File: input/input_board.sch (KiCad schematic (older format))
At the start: 21 parts, among them J2 MCLK, J4 SCKA, J5 SCKB, J6 SDOB1, U1 DS90LV048, U2 FIN1047, U5 74LVC541A

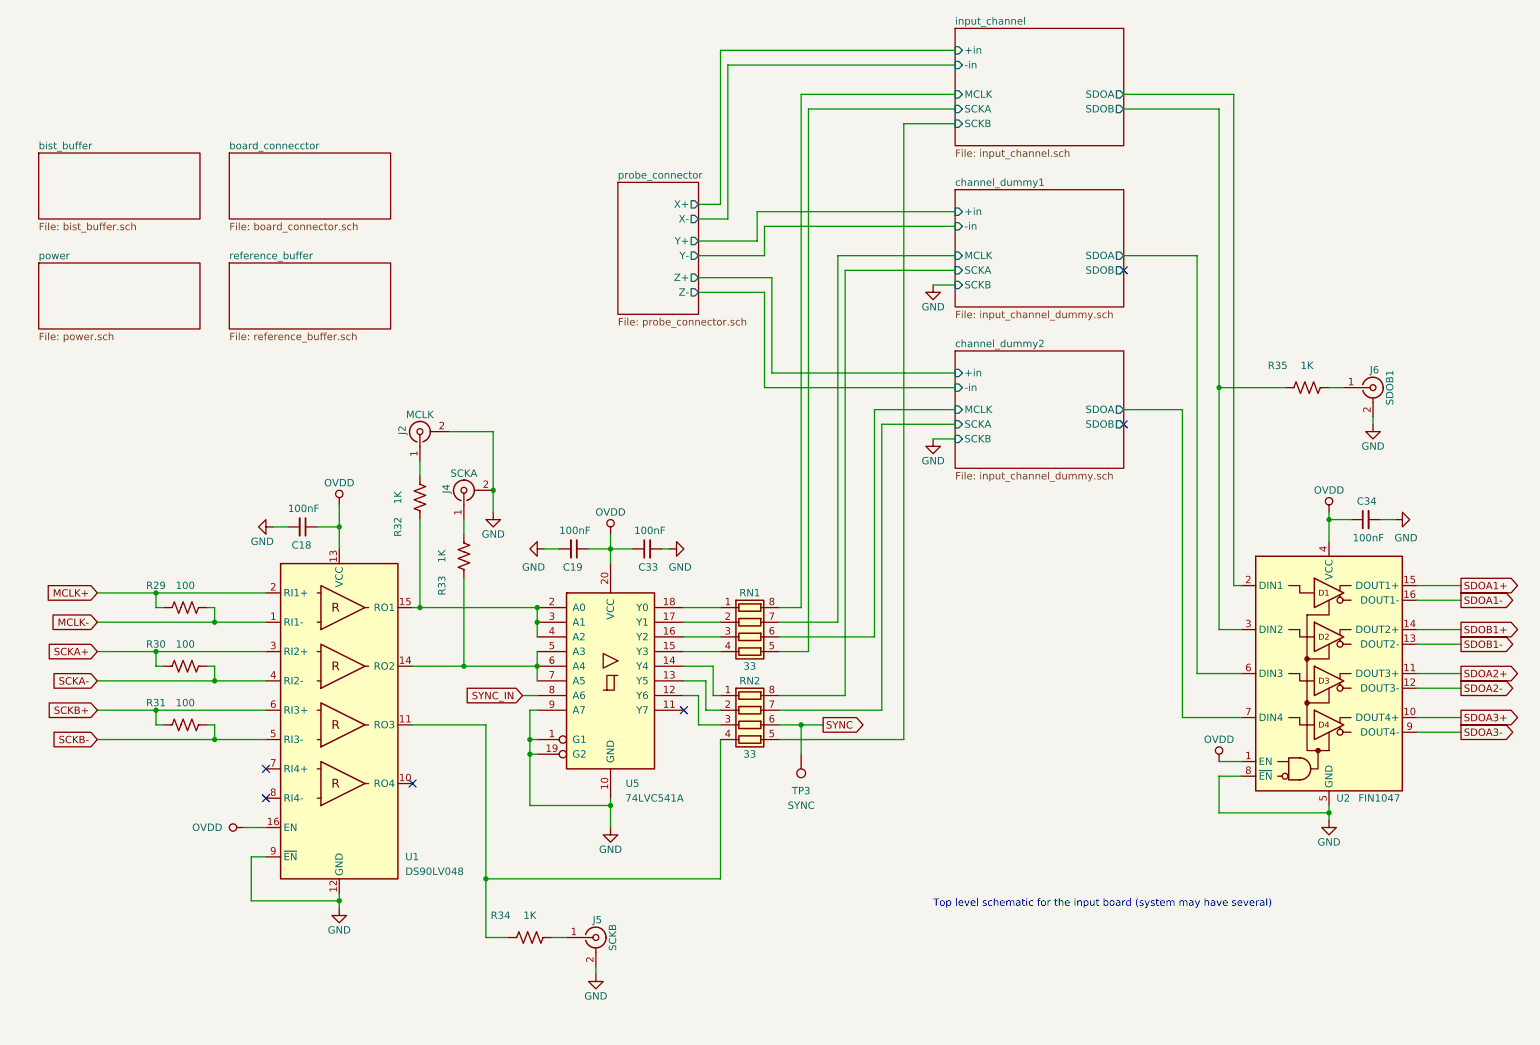
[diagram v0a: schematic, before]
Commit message: Lots of work on routing input_board.kicad_pcb, not done yet.
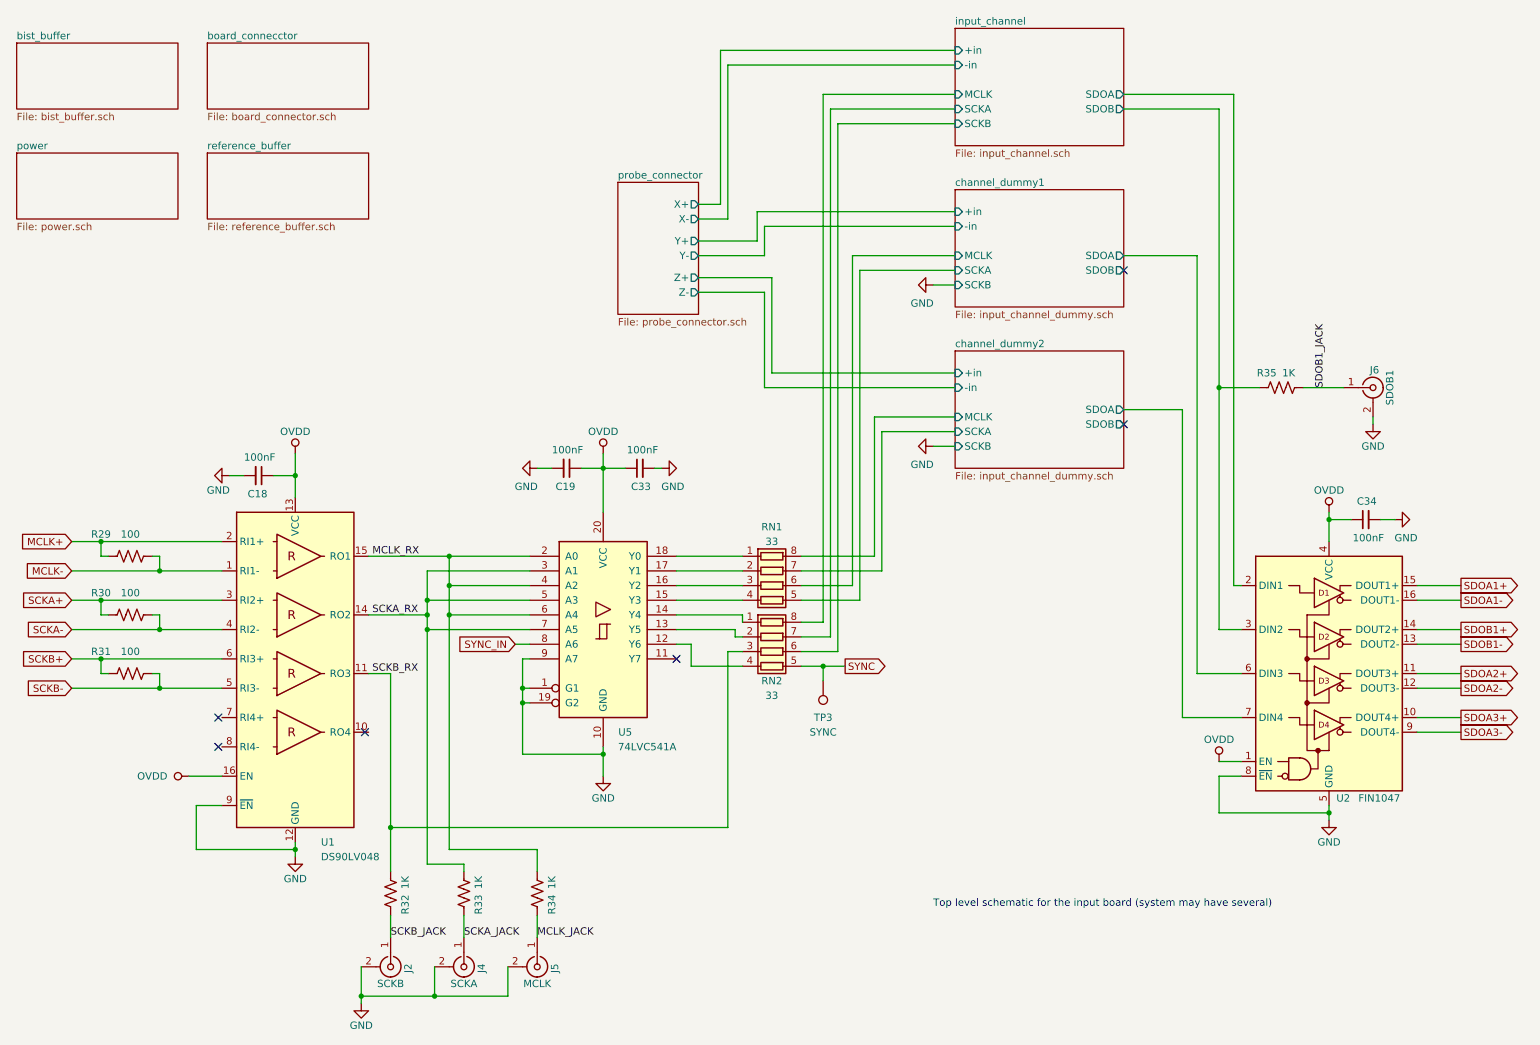
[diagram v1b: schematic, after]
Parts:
- J2: value MCLK -> SCKB
- J5: value SCKB -> MCLK
- U1: footprint Package_SO:SOIC-16_3.9x9.9mm_P1.27mm -> Package_SO:TSSOP-16_4.4x5mm_P0.65mm
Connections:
- net SYNC: now also RN2.5 (R4.2); no longer RN2.6 (R3.2)
- net channel_dummy1/MCLK: now also RN1.6 (R3.2); no longer RN1.7 (R2.2)
- net channel_dummy1/SCKA: now also RN1.5 (R4.2); no longer RN2.8 (R1.2)
- net channel_dummy2/MCLK: now also RN1.8 (R1.2); no longer RN1.6 (R3.2)
- net channel_dummy2/SCKA: now also RN1.7 (R2.2); no longer RN2.7 (R2.2)
- net input_channel/MCLK: now also RN2.8 (R1.2); no longer RN1.8 (R1.2)
- net input_channel/SCKA: now also RN2.7 (R2.2); no longer RN1.5 (R4.2)
- net input_channel/SCKB: now also RN2.6 (R3.2); no longer RN2.5 (R4.2)
- net at U5.12 (Y6): now also RN2.4 (R4.1); no longer RN2.3 (R3.1)
- net MCLK_RX: now reaches U1.15 (RO1), U5.2 (A0), U5.4 (A2)
- net MCLK_RX: now also R34.1, U5.6 (A4); no longer R32.1, U5.3 (A1)
- net SCKA_RX: now reaches R33.1, U1.14 (RO2), U5.5 (A3), U5.7 (A5)
- net SCKA_RX: now also U5.3 (A1); no longer U5.6 (A4)
- net SCKB_JACK: now reaches J2.1 (In), R32.2
- net SCKA_JACK: now reaches J4.1 (In), R33.2
- net MCLK_JACK: now reaches J5.1 (In), R34.2
- net SDOB1_JACK: now reaches J6.1 (In), R35.2
- new net SCKB_RX: R32.1, RN2.3 (R3.1), U1.11 (RO3)
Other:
- moved on the sheet: C18, C19, C33, J2, J4, J5, R29, R30, R31, R32, R33, R34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

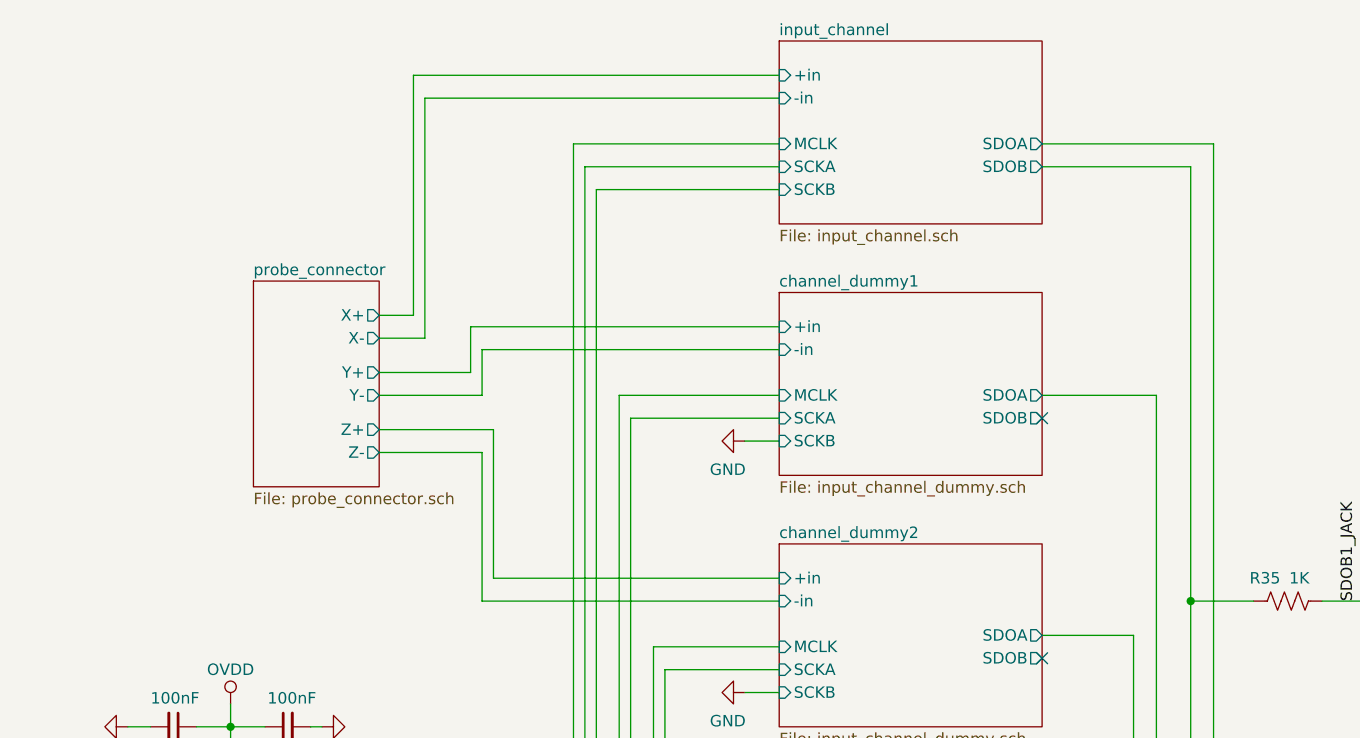
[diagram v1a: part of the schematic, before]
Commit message: Minor tweaks to schematic, and ongoing progress on PCB layout.
Changed BIST buffer to run off of CHAN1_V+, not the global V+.  This caused the CHAN_V+ net name to change.
On power.sch, added bypass caps for the VREF inputs to the V+/V- regulators.  Also, the BIST input lines now
have an RC filter, not just a resistor.
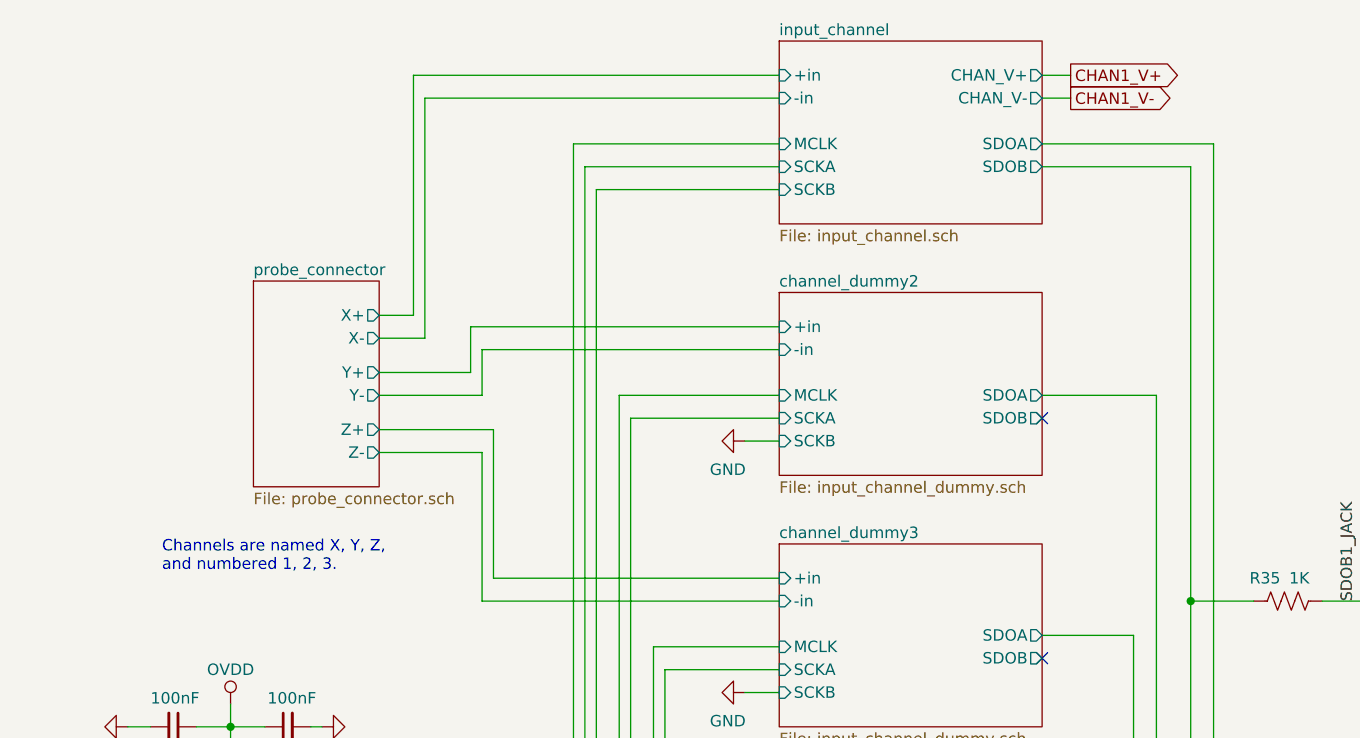
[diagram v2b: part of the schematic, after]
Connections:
- net channel_dummy1/MCLK is gone; now on net channel_dummy2/MCLK: RN1.6 (R3.2)
- net channel_dummy1/SCKA is gone; now on net channel_dummy2/SCKA: RN1.5 (R4.2)
- net channel_dummy1/SDOA is gone; now on net channel_dummy2/SDOA: U2.6 (DIN3)
- net channel_dummy2/MCLK: no longer RN1.8 (R1.2)
- net channel_dummy2/SCKA: no longer RN1.7 (R2.2)
- net channel_dummy2/SDOA: no longer U2.7 (DIN4)
- new net channel_dummy3/MCLK: RN1.8 (R1.2)
- new net channel_dummy3/SCKA: RN1.7 (R2.2)
- new net channel_dummy3/SDOA: U2.7 (DIN4)
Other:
- note added: "Channels are named X, Y, Z,\nand numbered 1, 2, 3."
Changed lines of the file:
@@
 F7 "SCKB" I L 7300 1500 50
 F8 "SCKA" I L 7300 1400 50
+F9 "CHAN_V+" O R 8450 1000 50
+F10 "CHAN_V-" O R 8450 1100 50
 $EndSheet
 $Sheet
 S 7300 1950 1150 800
 U 5E194E0B
-F0 "channel_dummy1" 50
+F0 "channel_dummy2" 50
 F1 "input_channel_dummy.sch" 50
 F2 "+in" I L 7300 2100 50
@@
 S 7300 3050 1150 800
 U 5E1F318C
-F0 "channel_dummy2" 50
+F0 "channel_dummy3" 50
 F1 "input_channel_dummy.sch" 50
 F2 "+in" I L 7300 3200 50
@@
 Text Label 9825 3300 1    50   ~ 0
 SDOB1_JACK
+Text GLabel 8575 1000 2    50   Output ~ 0
+CHAN1_V+
+Text GLabel 8575 1100 2    50   Output ~ 0
+CHAN1_V-
+Wire Wire Line
+	8575 1000 8450 1000
+Wire Wire Line
+	8575 1100 8450 1100
+Text Notes 4600 3175 0    50   ~ 0
+Channels are named X, Y, Z,\nand numbered 1, 2, 3.
 $EndSCHEMATC

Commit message: Snapshot before replicating input channels
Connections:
- net channel_dummy2/MCLK renamed channel2/MCLK
- net channel_dummy2/SCKA renamed channel2/SCKA
- net channel_dummy2/SDOA renamed channel2/SDOA
- net channel_dummy3/MCLK renamed channel3/MCLK
- net channel_dummy3/SCKA renamed channel3/SCKA
- net channel_dummy3/SDOA renamed channel3/SDOA
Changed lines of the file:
@@
 $Descr A4 11693 8268
 encoding utf-8
-Sheet 1 13
+Sheet 1 21
 Title ""
 Date ""
@@
 $EndSheet
 $Sheet
-S 7300 1950 1150 800
-U 5E194E0B
-F0 "channel_dummy2" 50
-F1 "input_channel_dummy.sch" 50
-F2 "+in" I L 7300 2100 50
-F3 "-in" I L 7300 2200 50
-F4 "SDOA" O R 8450 2400 50
-F5 "SDOB" O R 8450 2500 50
-F6 "MCLK" I L 7300 2400 50
-F7 "SCKB" I L 7300 2600 50
-F8 "SCKA" I L 7300 2500 50
-$EndSheet
-$Sheet
 S 2200 950  1100 450
 U 5E1D6729
@@
 Wire Wire Line
 	10450 5650 10750 5650
-$Sheet
-S 7300 3050 1150 800
-U 5E1F318C
-F0 "channel_dummy3" 50
-F1 "input_channel_dummy.sch" 50
-F2 "+in" I L 7300 3200 50
-F3 "-in" I L 7300 3300 50
-F4 "SDOA" O R 8450 3450 50
-F5 "SDOB" O R 8450 3550 50
-F6 "MCLK" I L 7300 3500 50
-F7 "SCKB" I L 7300 3700 50
-F8 "SCKA" I L 7300 3600 50
-$EndSheet
 Wire Wire Line
 	2800 6400 2800 6450
@@
 	9250 5550 8850 5550
 Wire Wire Line
-	8850 5550 8850 3450
-Wire Wire Line
-	8850 3450 8450 3450
+	8850 5550 8850 3500
+Wire Wire Line
+	8850 3500 8450 3500
 NoConn ~ 8450 2500
-NoConn ~ 8450 3550
 Wire Wire Line
 	5550 2050 5700 2050
@@
 Text Notes 4600 3175 0    50   ~ 0
 Channels are named X, Y, Z,\nand numbered 1, 2, 3.
+$Sheet
+S 7300 1950 1150 800
+U 5E448095
+F0 "channel2" 50
+F1 "input_channel.sch" 50
+F2 "+in" I L 7300 2100 50
+F3 "-in" I L 7300 2200 50
+F4 "SDOA" O R 8450 2400 50
+F5 "SDOB" O R 8450 2500 50
+F6 "MCLK" I L 7300 2400 50
+F7 "SCKB" I L 7300 2600 50
+F8 "SCKA" I L 7300 2500 50
+$EndSheet
+$Sheet
+S 7300 3050 1150 800
+U 5E45936E
+F0 "channel3" 50
+F1 "input_channel.sch" 50
+F2 "+in" I L 7300 3200 50
+F3 "-in" I L 7300 3300 50
+F4 "SDOA" O R 8450 3500 50
+F5 "SDOB" O R 8450 3600 50
+F6 "MCLK" I L 7300 3500 50
+F7 "SCKB" I L 7300 3700 50
+F8 "SCKA" I L 7300 3600 50
+$EndSheet
+NoConn ~ 8450 3600
 $EndSCHEMATC
